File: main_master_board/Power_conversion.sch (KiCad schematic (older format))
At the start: 0 parts

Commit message: Added power conversions for 12, 5, 3.3 from 24V
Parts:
- added C?: 10uF, Cin, symbol C
- added C?: 620pF, symbol C
- added C?: 22uF, symbol C
- added C?: 12pF, Cff, symbol C
- added C?: 2.2uF, Cin, symbol C
- added C?: 100nF, Cboot, symbol C
- added C?: 4.7uF, Cout, symbol C
- added C?: 68uF, symbol C
- added C?: 22uF, Cout, symbol C
- added D?: 0.55V, symbol D_Schottky
- added D?: BLUE_LED, symbol LED
- added D?: RED_LED, symbol LED
- added D?: GRN_LED, symbol LED
- added L?: 4.7uH, symbol L
- added R?: 523K, symbol R
- added R? (x2): 100K, symbol R
- added R?: 10.5K, Rt, symbol R
- added R?: 150K, Rfbt, symbol R
- added R?: 10K, Rfbb, symbol R
- added R?: 10K, symbol R
- added R?: 10K, Rup, symbol R
- added R?: 150K, Rreft, symbol R
- added R?: 10K, Rrefb, symbol R
- added R? (x3): 330, Rled, symbol R
- added U?: TPS832130SIL, MODULE, symbol TPS832130SIL
- added U?: LMR16020, MODULE, symbol LMR16020
- added U?: TPS754, MODULE, symbol TPS754
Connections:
- net labels added: 3V3, 3V3_en, 3V3_out, GND, Pullup_ref, V12, V12_out, V24, V24_in, V5, V5_out, arm_en, v12_good
- wire segments 0 -> 147
- no-connect marks 0 -> 8
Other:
- note added: "12V to 5V Buck"
- note added: "24V to 12V Buck"
- note added: "5V to 3.3V LDO"
- note added: "Check resistor value!"
- note added: "Sheet Inputs"
- note added: "Sheet Outputs"

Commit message: Working on adding boost converter
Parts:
- added C?: 100nF, Cin2, symbol C_Small
- added C?: 2.2uF, Cvcc, symbol C_Small
- added C?: 9.10pF, Ccomp2, symbol C_Small
- added C?: 180pF, Ccomp, symbol C_Small
- added C? (x3): 10uF, Cin, symbol C_Small
- added C?: 100nF, Cbst, symbol C_Small
- added C? (x2): 10uF, Cout, symbol C_Small
- added L?: 470nH, symbol L
- added R?: 69.8K, Rcomp, symbol R
- added R?: 158K, Rlim, symbol R
- added R?: 82K, Rt, symbol R
- added R?: 1.05M, Rfbt, symbol R
- added R?: 118K, Rfbb, symbol R
- added U?: TPS61089, MODULE, symbol TPS61089
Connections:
- net labels added: V4, Vbackup, Vmain
- net labels removed: V24_in
- wire segments 147 -> 151
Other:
- note added: "All the\nsame\ncapacitor"
- moved on the sheet: C?, D?, L?, R?, U?

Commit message: Finished Boost and working on power switching. LDO needs to be changed
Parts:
- removed D?: BLUE_LED, symbol LED
- added D? (x2): BLUE_LED, VLMB1310-GS08CT-ND, symbol LED-RESCUE-main_master_board
- added R?: 267K, Rreft, symbol R
- added R?: 102K, Rrefb, symbol R
- added R?: 200, Rled, symbol R
- added R?: 102K, Rreft, symbol R
- added R?: 68.1K, Rrefb, symbol R
- added R? (x4): 50k, symbol R
- added U? (x2): FDS4935A, symbol FDS4935A
- added U?: Si1900DL, MODULE, symbol Si1900DL
- D?: footprint (none) -> 732-4978-1-ND; symbol LED -> LED-RESCUE-main_master_board
- D?: footprint (none) -> 754-1126-1-ND; symbol LED -> LED-RESCUE-main_master_board
- R?: value 150K -> 267K
- R?: value 10K -> 102K
- R? (x3): value 330 -> 200
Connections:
- net labels added: FET_Power_on, Main_enable, P_ref_boo, P_ref_buc, Switch_on, V12_BACKUP, V12_MAIN, V12_MERGE, v5_good, v5_ref, ~arm_en
- net labels removed: Pullup_ref, arm_en
- wire segments 151 -> 199
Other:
- note added: "4.2V to 12V Boost"
- note removed: "Check resistor value!"
- moved on the sheet: C?, L?, R?, U?

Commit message: Added Power Board library from SBv1 and updated the power sch and started saftey switches
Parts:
- removed C?: 22uF, symbol C
- removed C?: 68uF, symbol C
- removed R?: 10K, symbol R
- removed R?: 50k, symbol R
- removed U?: TPS754, MODULE, symbol TPS754
- added C?: 22uF, symbol C
- added C?: 22uF, symbol CP1
- added S?: SWITCH_DPDT, symbol SWITCH_DPDT
- added U?: Si1900DL, MODULE, symbol Si1900DL
- added U?: LP3852-3.3, MODULE, symbol LP3852-3.3
- R?: value 50k -> 10k
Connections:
- net labels added: PFET_ON
- net labels removed: 3V3_en, FET_Power_on, Main_enable, ~arm_en
- wire segments 199 -> 191
- no-connect marks 8 -> 0
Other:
- note added: "12V Switch Between Main Buck and Backup Boost"
- moved on the sheet: R?, U?

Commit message: Added lots of things. current/voltage monitoring. and other stuff
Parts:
- added C? (x3): 100nF, symbol C_Small
- added C?: 4.7uF, symbol C_Small
- added D?: UCLAMP1211P, symbol D_TVS
- added D?: uClamp0511P, symbol D_TVS
- added D?: uClamp3311P, symbol D_TVS
- added D?: GRN_LED, 754-1126-1-ND, symbol LED-RESCUE-main_master_board
- added F?: PTS181212V150, symbol Fuse_Small
- added F? (x2): PTC Fuse, symbol Fuse_Small
- added IC?: IC_MCP73831, dp_devices-SOT-23-5, symbol IC_MCP73831
- added R? (x3): 0.02, symbol R
- added R? (x2): 10k, symbol R_Small
- added R?: 2K, symbol R_Small
- added R? (x3): 10K, symbol R_Small
- added R?: 6.2k, symbol R_Small
- added R?: 200, Rled, symbol R
- added U? (x3): INA197, symbol INA197
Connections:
- net labels added: 3V3_FUSE, 3V3_cur, 3V3_volt, V12_FUSE, V12_cur, V12_volt, V5_FUSE, V5_cur, V5_volt, charge_on, charging
- wire segments 191 -> 277
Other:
- note added: "Coverted Power Fuses and Current Monitoring"
- note added: "Voltage \nMonitoring"
- moved on the sheet: C?, D?, R?, U?

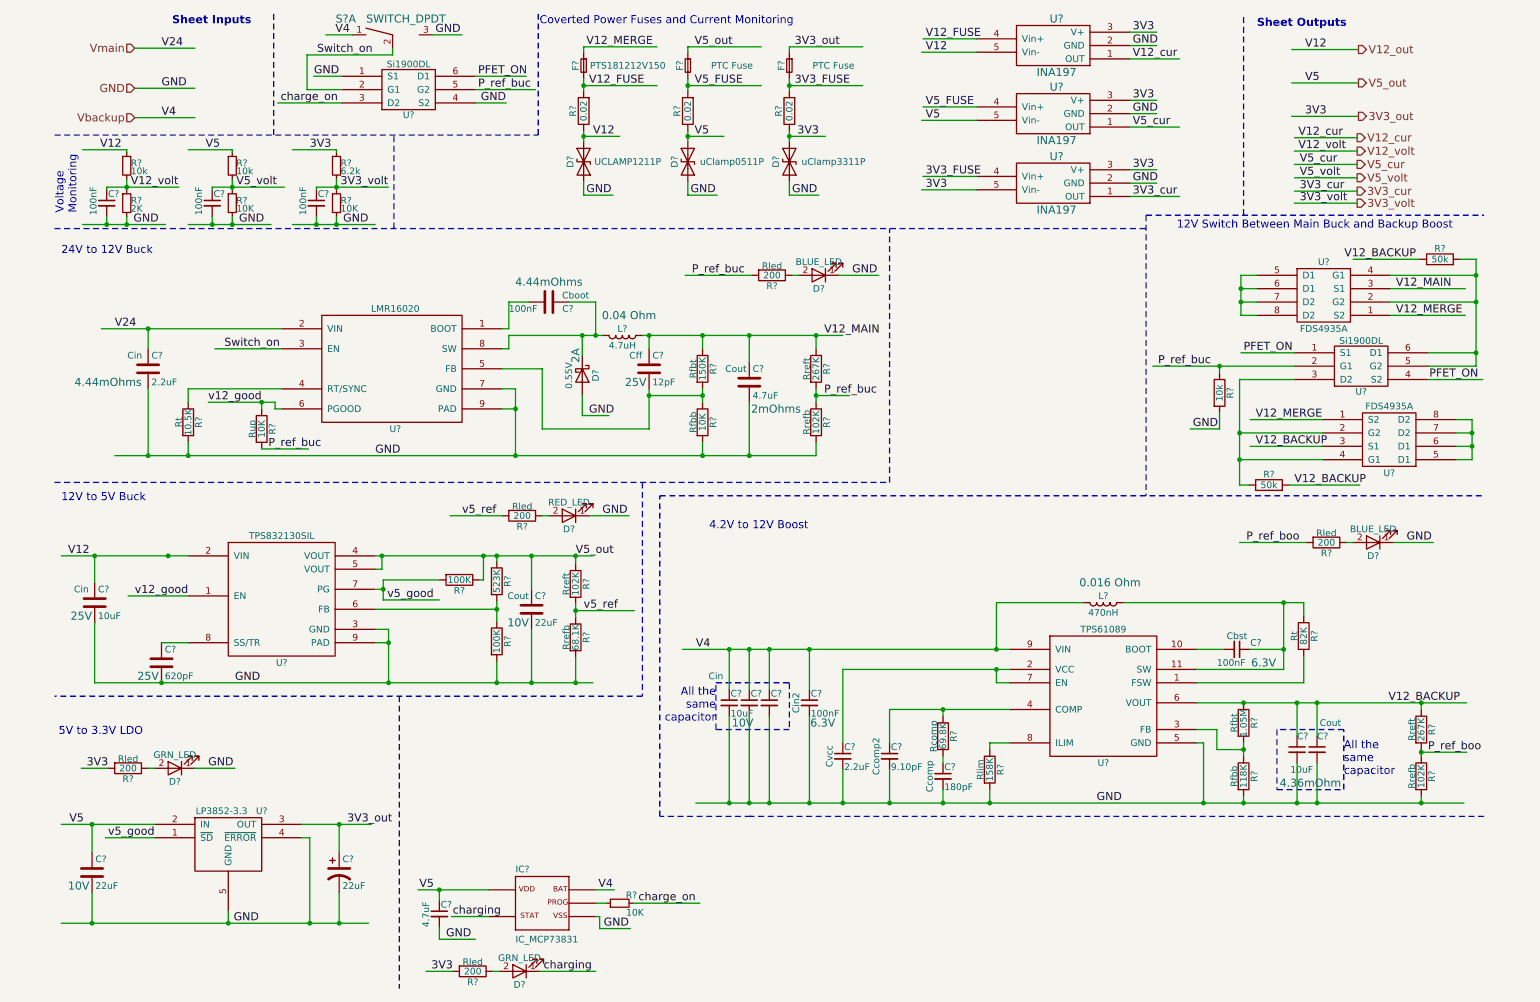
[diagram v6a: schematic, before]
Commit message: Added output cap on 1s charger.
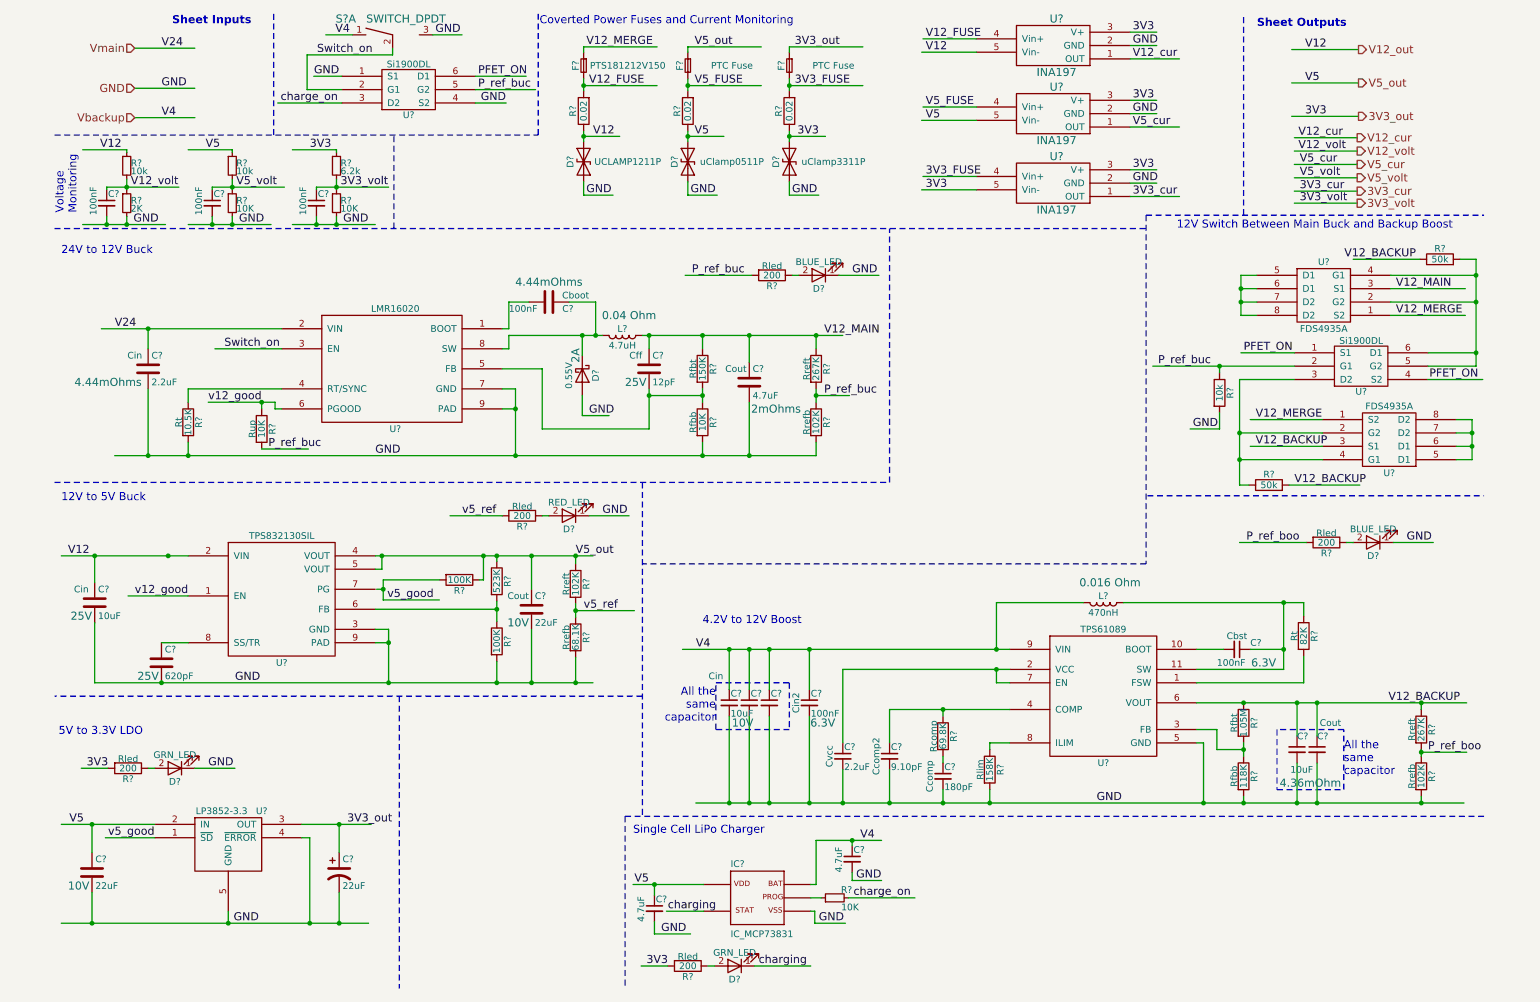
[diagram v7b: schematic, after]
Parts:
- added C?: 4.7uF, symbol C_Small
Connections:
- wire segments 277 -> 282
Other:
- note added: "Single Cell LiPo Charger"
- moved on the sheet: C?, D?, IC?, R?
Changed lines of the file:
@@
 Text Label 3550 4250 0    60   ~ 0
 v5_ref
-Text Notes 5400 4360 0    60   ~ 0
+Text Notes 5350 5070 0    60   ~ 0
 4.2V to 12V Boost
 $Comp
@@
 L IC_MCP73831 IC?
 U 1 1 58758461
-P 4150 7150
-F 0 "IC?" H 3950 7375 50  0000 L BNN
-F 1 "IC_MCP73831" H 3950 6850 50  0000 L BNN
-F 2 "dp_devices-SOT-23-5" H 4150 7300 50  0001 C CNN
-F 3 "" H 4150 7150 60  0001 C CNN
-	1    4150 7150
-	1    0    0    -1
-$EndComp
-Text Label 3480 7250 0    60   ~ 0
+P 5760 7110
+F 0 "IC?" H 5560 7335 50  0000 L BNN
+F 1 "IC_MCP73831" H 5560 6810 50  0000 L BNN
+F 2 "dp_devices-SOT-23-5" H 5760 7260 50  0001 C CNN
+F 3 "" H 5760 7110 60  0001 C CNN
+	1    5760 7110
+	1    0    0    -1
+$EndComp
+Text Label 5090 7210 0    60   ~ 0
 charging
 Text Label 1650 6140 0    60   ~ 0
@@
 L LED-RESCUE-main_master_board D?
 U 1 1 5875ED3E
-P 3980 7660
-F 0 "D?" H 3980 7760 50  0000 C CNN
-F 1 "GRN_LED" H 3980 7560 50  0000 C CNN
-F 2 "754-1126-1-ND" H 3980 7660 50  0001 C CNN
-F 3 "http://www.digikey.com/product-detail/en/kingbright/APT1608ZGC/754-1126-1-ND" H 3980 7660 50  0001 C CNN
-	1    3980 7660
+P 5590 7620
+F 0 "D?" H 5590 7720 50  0000 C CNN
+F 1 "GRN_LED" H 5590 7520 50  0000 C CNN
+F 2 "754-1126-1-ND" H 5590 7620 50  0001 C CNN
+F 3 "http://www.digikey.com/product-detail/en/kingbright/APT1608ZGC/754-1126-1-ND" H 5590 7620 50  0001 C CNN
+	1    5590 7620
 	-1   0    0    1
 $EndComp
@@
 L R R?
 U 1 1 5875ED44
-P 3630 7660
-F 0 "R?" V 3710 7660 50  0000 C CNN
-F 1 "200" V 3630 7660 50  0000 C CNN
-F 2 "Rled" V 3560 7660 50  0000 C CNN
-F 3 "" H 3630 7660 50  0000 C CNN
-	1    3630 7660
+P 5240 7620
+F 0 "R?" V 5320 7620 50  0000 C CNN
+F 1 "200" V 5240 7620 50  0000 C CNN
+F 2 "Rled" V 5170 7620 50  0000 C CNN
+F 3 "" H 5240 7620 50  0000 C CNN
+	1    5240 7620
 	0    1    1    0
 $EndComp
-Text Label 3320 7660 0    60   ~ 0
+Text Label 4930 7620 0    60   ~ 0
 3V3
-Text Label 4160 7660 0    60   ~ 0
+Text Label 5770 7620 0    60   ~ 0
 charging
-Text Label 3430 7420 0    60   ~ 0
+Text Label 5040 7380 0    60   ~ 0
 GND
 $Comp
 L C_Small C?
 U 1 1 58761A6D
-P 3380 7230
-F 0 "C?" H 3390 7300 50  0000 L CNN
-F 1 "4.7uF" V 3280 7130 50  0000 L CNN
-F 2 "" H 3380 7230 50  0000 C CNN
-F 3 "" H 3380 7230 50  0000 C CNN
-	1    3380 7230
-	1    0    0    -1
-$EndComp
-Text Label 3230 7050 0    60   ~ 0
+P 4990 7190
+F 0 "C?" H 5000 7260 50  0000 L CNN
+F 1 "4.7uF" V 4890 7090 50  0000 L CNN
+F 2 "" H 4990 7190 50  0000 C CNN
+F 3 "" H 4990 7190 50  0000 C CNN
+	1    4990 7190
+	1    0    0    -1
+$EndComp
+Text Label 4840 7010 0    60   ~ 0
 V5
 $Comp
 L R_Small R?
 U 1 1 58763DBB
-P 4730 7150
-F 0 "R?" V 4790 7020 50  0000 L CNN
-F 1 "10K" V 4660 6970 50  0000 L CNN
-F 2 "" H 4730 7150 50  0000 C CNN
-F 3 "" H 4730 7150 50  0000 C CNN
-	1    4730 7150
+P 6340 7110
+F 0 "R?" V 6400 6980 50  0000 L CNN
+F 1 "10K" V 6270 6930 50  0000 L CNN
+F 2 "" H 6340 7110 50  0000 C CNN
+F 3 "" H 6340 7110 50  0000 C CNN
+	1    6340 7110
 	0    -1   -1   0
 $EndComp
-Text Label 4610 7340 0    60   ~ 0
-GND
-Text Label 4570 7050 0    60   ~ 0
-V4
-Text Label 4870 7150 0    60   ~ 0
+Text Label 6220 7300 0    60   ~ 0
+GND
+Text Label 6480 7110 0    60   ~ 0
 charge_on
 Text Label 2620 1160 2    60   ~ 0
@@
 	500  1400 2350 1400
 Wire Notes Line
-	8670 2000 8670 4100
+	8670 2000 8670 4610
 Connection ~ 780  6560
 Connection ~ 2630 6560
@@
 	9400 2000 9400 500
 Wire Notes Line
-	4900 4000 4900 5600
+	4900 4000 4900 6500
 Wire Notes Line
 	4900 5600 500  5600
@@
 Wire Notes Line
 	11200 6500 5700 6500
-Wire Notes Line
-	5030 4100 11200 4100
 Wire Wire Line
 	1100 1270 1550 1270
@@
 Connection ~ 4400 4960
 Wire Notes Line
-	5710 6500 5030 6500
-Wire Notes Line
-	5030 6500 5030 4100
+	4770 6500 5710 6500
 Wire Wire Line
 	11110 3530 11110 3830
@@
 	10250 1910 9780 1910
 Wire Wire Line
-	3750 7250 3470 7250
-Wire Wire Line
-	3280 7660 3480 7660
-Wire Wire Line
-	4130 7660 4550 7660
-Wire Wire Line
-	3780 7660 3830 7660
-Wire Wire Line
-	3380 7420 3650 7420
-Wire Wire Line
-	3220 7050 3750 7050
-Wire Wire Line
-	3380 7130 3380 7050
-Connection ~ 3380 7050
-Wire Wire Line
-	3380 7330 3380 7420
-Wire Wire Line
-	4550 7150 4630 7150
-Wire Wire Line
-	4830 7150 5330 7150
-Wire Wire Line
-	4550 7050 4690 7050
-Wire Wire Line
-	4550 7250 4580 7250
-Wire Wire Line
-	4580 7250 4580 7340
-Wire Wire Line
-	4580 7340 4810 7340
+	5360 7210 5080 7210
+Wire Wire Line
+	4890 7620 5090 7620
+Wire Wire Line
+	5740 7620 6160 7620
+Wire Wire Line
+	5390 7620 5440 7620
+Wire Wire Line
+	4990 7380 5260 7380
+Wire Wire Line
+	4830 7010 5360 7010
+Wire Wire Line
+	4990 7090 4990 7010
+Connection ~ 4990 7010
+Wire Wire Line
+	4990 7290 4990 7380
+Wire Wire Line
+	6160 7110 6240 7110
+Wire Wire Line
+	6440 7110 6940 7110
+Wire Wire Line
+	6160 7210 6190 7210
+Wire Wire Line
+	6190 7210 6190 7300
+Wire Wire Line
+	6190 7300 6420 7300
 Wire Wire Line
 	2650 1160 2170 1160
@@
 Wire Notes Line
 	2140 1400 2140 480
+$Comp
+L C_Small C?
+U 1 1 58733778
+P 6470 6820
+F 0 "C?" H 6480 6890 50  0000 L CNN
+F 1 "4.7uF" V 6370 6720 50  0000 L CNN
+F 2 "" H 6470 6820 50  0000 C CNN
+F 3 "" H 6470 6820 50  0000 C CNN
+	1    6470 6820
+	1    0    0    -1
+$EndComp
+Wire Wire Line
+	6160 7010 6200 7010
+Wire Wire Line
+	6200 7010 6200 6680
+Wire Wire Line
+	6200 6680 6690 6680
+Wire Wire Line
+	6470 6680 6470 6720
+Connection ~ 6470 6680
+Wire Wire Line
+	6470 6920 6470 6980
+Wire Wire Line
+	6470 6980 6690 6980
+Text Label 6500 6980 0    60   ~ 0
+GND
+Text Label 6530 6680 0    60   ~ 0
+V4
+Wire Notes Line
+	4770 6500 4770 7780
+Text Notes 4830 6640 0    60   ~ 0
+Single Cell LiPo Charger
+Wire Notes Line
+	8670 4610 4900 4610
+Wire Notes Line
+	8680 4100 11200 4100
 $EndSCHEMATC

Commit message: Updated some of the schematics and started assigning footprints
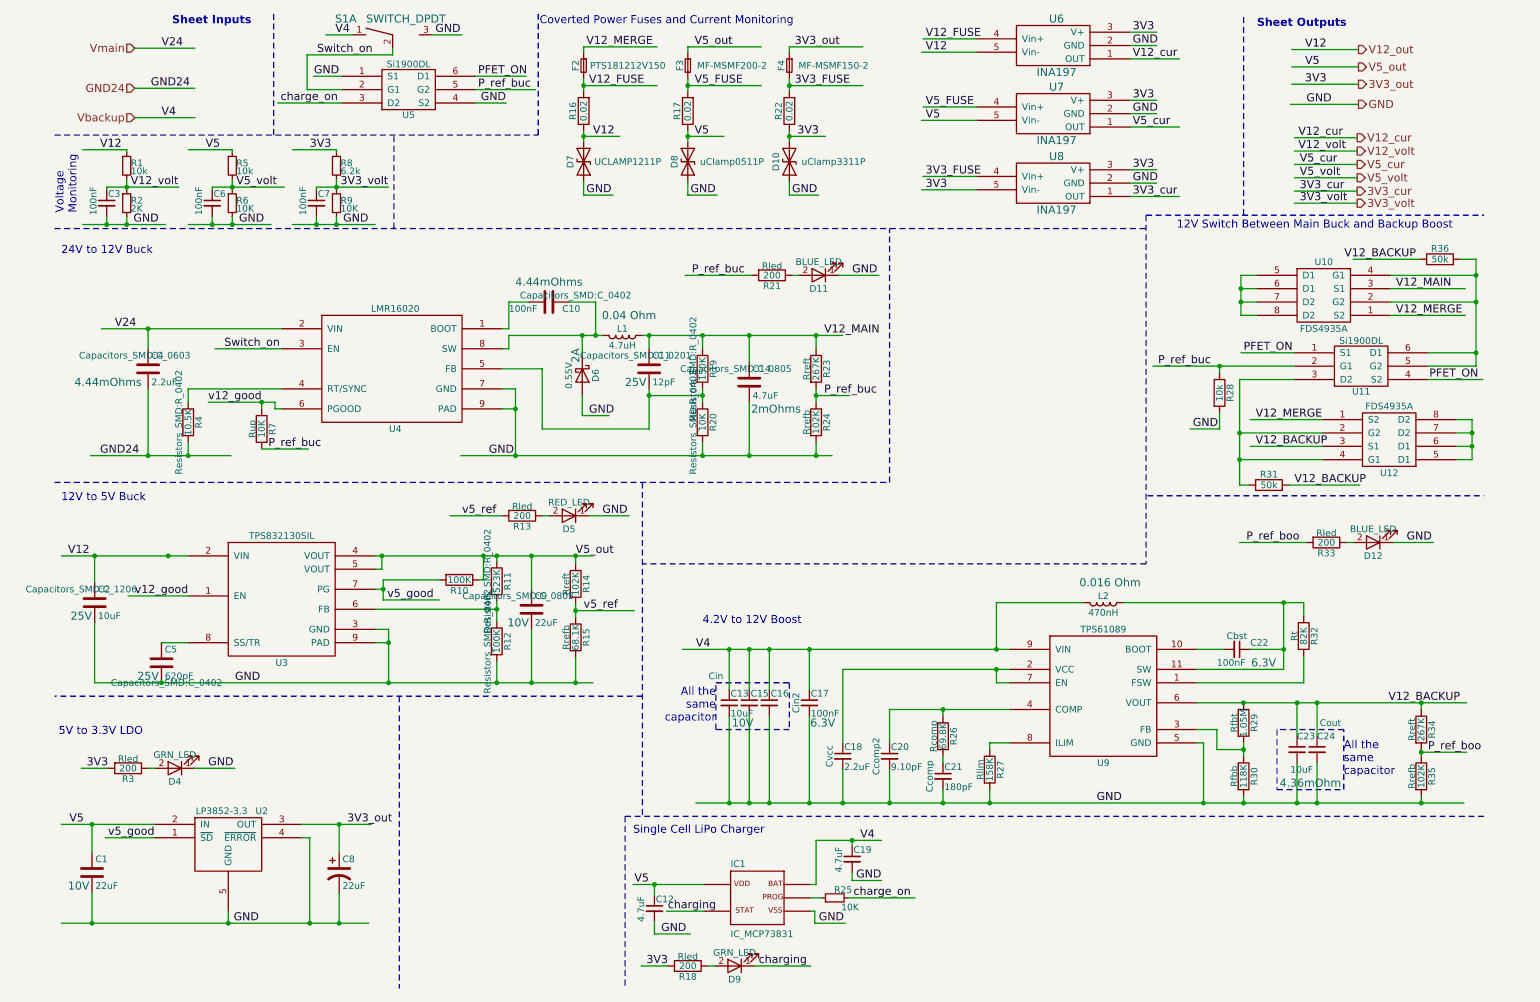
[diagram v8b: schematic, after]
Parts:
- C1, C3, C6, C7, C8: renamed from C?; footprint (none) -> Capacitors_SMD:C_0603
- C10: renamed from C?; footprint Cboot -> Capacitors_SMD:C_0402; Field5 (none) -> C1005X7R1H104K
- C11: renamed from C?; footprint Cff -> Capacitors_SMD:C_0201; Field5 (none) -> C0201C120K3GACTU
- C14: renamed from C?; footprint Cout -> Capacitors_SMD:C_0805; Field5 (none) -> GRM21BR61E475MA12L
- C2: renamed from C?; footprint Cin -> Capacitors_SMD:C_1206; Field5 (none) -> TMK316BJ106KL-T
- C4: renamed from C?; footprint Cin -> Capacitors_SMD:C_0603; Field5 (none) -> GRM31CR71H225KA88L
- C5: renamed from C?; footprint (none) -> Capacitors_SMD:C_0402; Field5 (none) -> GRM1555C1E621JA01D
- C9: renamed from C?; footprint Cout -> Capacitors_SMD:C_0805; Field5 (none) -> LMK212BJ226MG-T
- D6: renamed from D?; footprint (none) -> Diodes_SMD:SOD-123; Field5 (none) -> SS24FL
- F3: renamed from F?; value PTC Fuse -> MF-MSMF200-2
- F4: renamed from F?; value PTC Fuse -> MF-MSMF150-2
- IC1: renamed from IC?; footprint dp_devices-SOT-23-5 -> dp_devices:dp_devices-SOT-23-5
- L1: renamed from L?; footprint (none) -> Inductors:Inductor_Wurth_MAPI-4020; Field5 (none) -> XAL4030-472MEB
- R11: renamed from R?; footprint (none) -> Resistors_SMD:R_0402; Field4 (none) -> d; Field5 (none) -> CRCW0402523KFKED
- R12: renamed from R?; footprint (none) -> Resistors_SMD:R_0402; Field4 (none) -> d; Field5 (none) -> CRCW0402100KFKED
- R19: renamed from R?; footprint Rfbt -> Resistors_SMD:R_0402; Field4 (none) -> d; Field5 (none) -> CRCW0402150KFKED
- R20: renamed from R?; footprint Rfbb -> Resistors_SMD:R_0402; Field4 (none) -> d; Field5 (none) -> CRCW040210K0FKED
- R4: renamed from R?; footprint Rt -> Resistors_SMD:R_0402; Field4 (none) -> d; Field5 (none) -> CRCW040210K5FKED
- U3: renamed from U?; footprint MODULE -> uSIP-8:uSIP-8
- U4: renamed from U?; footprint MODULE -> HSOIC-8:HSOIC-8-1EP_Pitch1.27mm; Field4 (none) -> d; Field5 (none) -> LMR16020PDDAR
- gave numbers to parts that had none: 63
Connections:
- net labels added: GND24
- wire segments 282 -> 382
